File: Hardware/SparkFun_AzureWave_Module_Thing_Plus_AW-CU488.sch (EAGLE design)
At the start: 60 parts, among them J1 THING_PLUS, J2 LiPo, J3 QWIIC_RA, J5 USB-C, Q1 3.1A/30V/105mΩ, Q2 MBT3904DW1T1, U1 AW-CU488, U2 CP210X, U3 XC6222B331MR-G, U4 MCP73831

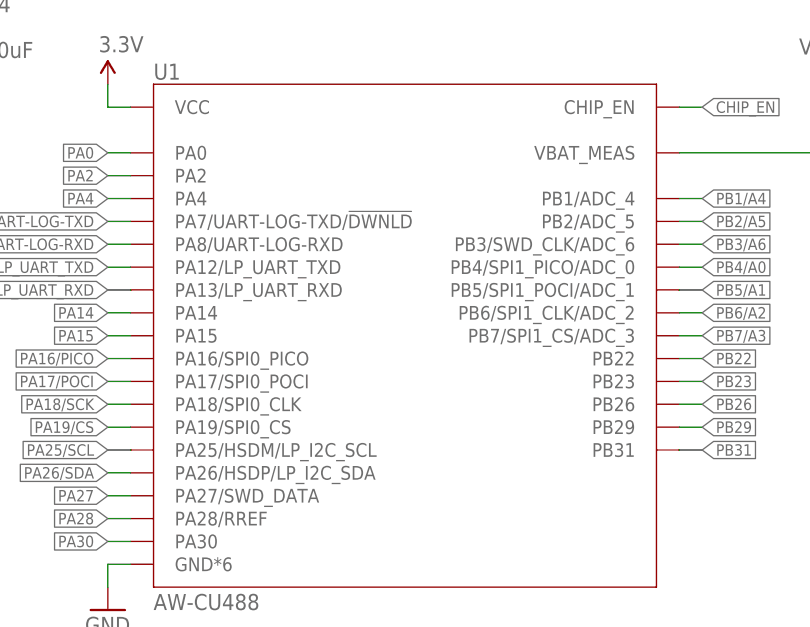
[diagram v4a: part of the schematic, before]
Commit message: audio codec specific pin-names into sch symbol
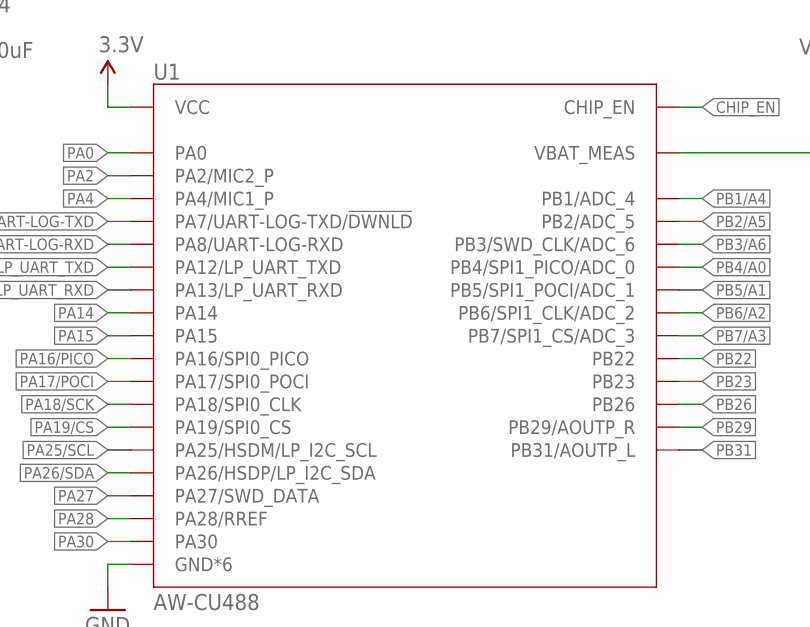
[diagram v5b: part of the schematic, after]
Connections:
- net PA2: now also U1.PA2/MIC2_P; no longer U1.PA2
- net PA4: now also U1.PA4/MIC1_P; no longer U1.PA4
- net PB29: now also U1.PB29/AOUTP_R; no longer U1.PB29
- net PB31: now also U1.PB31/AOUTP_L; no longer U1.PB31
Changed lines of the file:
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@@
 <wire x1="40.64" y1="124.46" x2="38.1" y2="124.46" width="0.1524" layer="91"/>
 <label x="38.1" y="124.46" size="1.27" layer="95" font="vector" rot="R180" xref="yes"/>
-<pinref part="U1" gate="U1" pin="PA2"/>
+<pinref part="U1" gate="U1" pin="PA2/MIC2_P"/>
 </segment>
 <segment>
@@
 <wire x1="40.64" y1="121.92" x2="38.1" y2="121.92" width="0.1524" layer="91"/>
 <label x="38.1" y="121.92" size="1.27" layer="95" font="vector" rot="R180" xref="yes"/>
-<pinref part="U1" gate="U1" pin="PA4"/>
+<pinref part="U1" gate="U1" pin="PA4/MIC1_P"/>
 </segment>
 <segment>
@@
 <net name="PB29" class="0">
 <segment>
-<pinref part="U1" gate="U1" pin="PB29"/>
+<pinref part="U1" gate="U1" pin="PB29/AOUTP_R"/>
 <wire x1="101.6" y1="96.52" x2="104.14" y2="96.52" width="0.1524" layer="91"/>
 <label x="104.14" y="96.52" size="1.27" layer="95" font="vector" xref="yes"/>
@@
 <net name="PB31" class="0">
 <segment>
-<pinref part="U1" gate="U1" pin="PB31"/>
+<pinref part="U1" gate="U1" pin="PB31/AOUTP_L"/>
 <wire x1="101.6" y1="93.98" x2="104.14" y2="93.98" width="0.1524" layer="91"/>
 <label x="104.14" y="93.98" size="1.27" layer="95" font="vector" xref="yes"/>
